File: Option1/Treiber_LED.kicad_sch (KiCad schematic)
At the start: 2 parts, among them Q601 AON6284

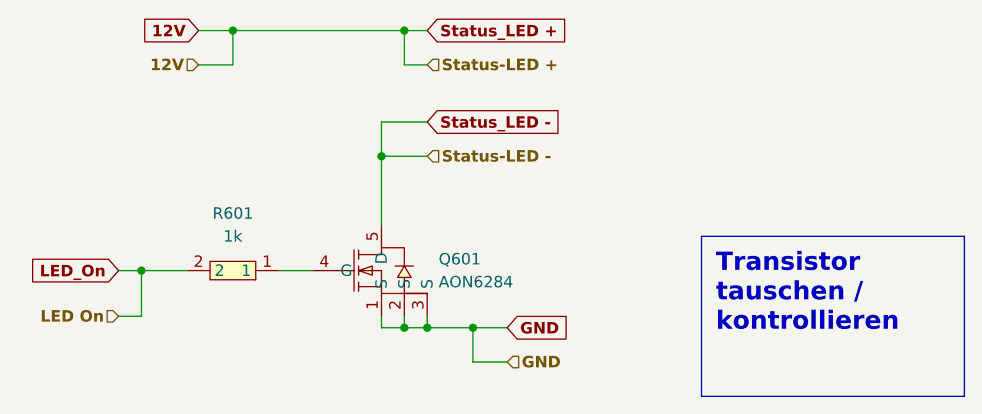
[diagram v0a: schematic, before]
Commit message: SPI Flash hinzugefügt, IN/Outputs vereinheitlicht, USB Flash Möglichkeit hinzugefügt, Display fehtl noch
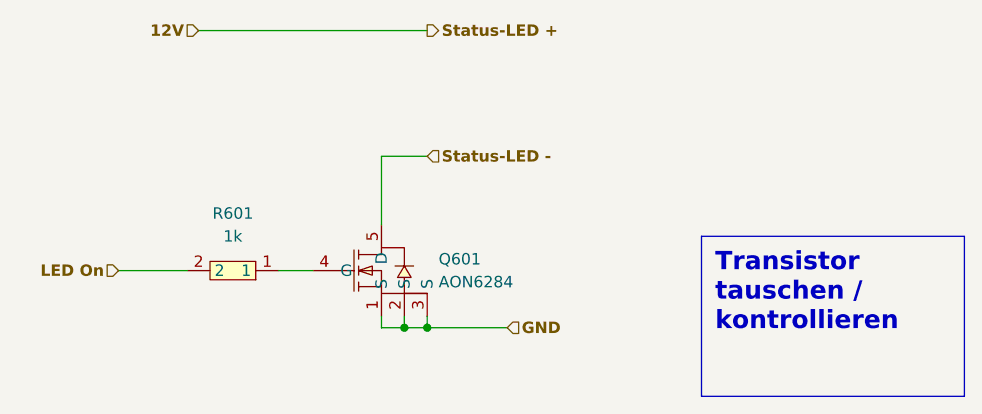
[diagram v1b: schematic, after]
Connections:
- net LED_On renamed LED On
- net Status_LED - renamed Status-LED -

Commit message: USB auf 3V3 umgebaut
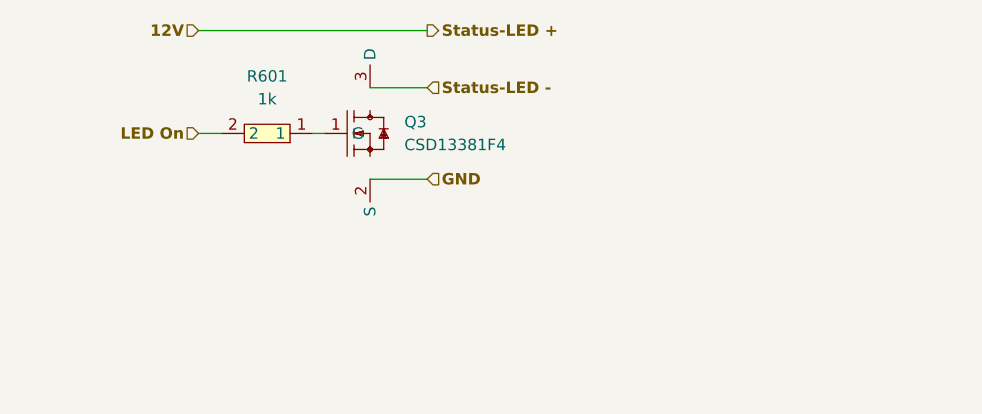
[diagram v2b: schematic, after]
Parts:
- removed Q601: AON6284, easyeda2kicad:POWERVDFN-8_L6.2-W5.2-P1.27-LS6.0-BL, symbol easyeda2kicad:AON6284
- added Q3: CSD13381F4, easyeda2kicad:PICOSTAR-3_L1.0-W0.6-P0.40-S0.65-BL-1, symbol EasyEda2KiCad:CSD13381F4
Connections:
- net GND: now also Q3.2 (S)
- net Status-LED -: now also Q3.3 (D)
- net at R601.1: now also Q3.1 (G)
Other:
- moved on the sheet: R601
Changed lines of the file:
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@@
 		)
 	)
-	(text_box "Transistor tauschen / kontrollieren"
-		(exclude_from_sim no)
-		(at 185.42 96.52 0)
-		(size 29.21 17.78)
-		(margins 1.524 1.524 1.524 1.524)
-		(stroke
-			(width 0)
-			(type default)
-			(color 247 0 0 1)
-		)
-		(fill
-			(type none)
-		)
-		(effects
-			(font
-				(size 2.032 2.032)
-				(thickness 0.4064)
-				(bold yes)
-				(color 247 0 0 1)
-			)
-			(justify left top)
-		)
-	)
-	(junction
-		(at 154.94 106.68)
-		(diameter 0)
-		(color 0 0 0 0)
-	)
-	(junction
-		(at 152.4 106.68)
-		(diameter 0)
-		(color 0 0 0 0)
-	)
-	(wire
-		(pts
-			(xy 154.94 106.68) (xy 152.4 106.68)
-		)
-		(stroke
-			(width 0)
-			(type default)
-		)
-	)
-	(wire
-		(pts
-			(xy 138.43 100.33) (xy 142.24 100.33)
+	(wire
+		(pts
+			(xy 143.51 85.09) (xy 142.24 85.09)
 		)
 		(stroke
@@
 	(wire
 		(pts
-			(xy 152.4 105.41) (xy 152.4 106.68)
-		)
-		(stroke
-			(width 0)
-			(type default)
-		)
-	)
-	(wire
-		(pts
-			(xy 149.86 106.68) (xy 149.86 105.41)
-		)
-		(stroke
-			(width 0)
-			(type default)
-		)
-	)
-	(wire
-		(pts
-			(xy 154.94 105.41) (xy 154.94 106.68)
-		)
-		(stroke
-			(width 0)
-			(type default)
-		)
-	)
-	(wire
-		(pts
-			(xy 152.4 106.68) (xy 149.86 106.68)
-		)
-		(stroke
-			(width 0)
-			(type default)
-		)
-	)
-	(wire
-		(pts
-			(xy 149.86 87.63) (xy 154.94 87.63)
-		)
-		(stroke
-			(width 0)
-			(type default)
-		)
-	)
-	(wire
-		(pts
-			(xy 120.65 100.33) (xy 128.27 100.33)
-		)
-		(stroke
-			(width 0)
-			(type default)
-		)
-	)
-	(wire
-		(pts
-			(xy 154.94 106.68) (xy 163.83 106.68)
-		)
-		(stroke
-			(width 0)
-			(type default)
-		)
-	)
-	(wire
-		(pts
-			(xy 149.86 87.63) (xy 149.86 95.25)
+			(xy 148.59 90.17) (xy 154.94 90.17)
+		)
+		(stroke
+			(width 0)
+			(type default)
+		)
+	)
+	(wire
+		(pts
+			(xy 148.59 80.01) (xy 154.94 80.01)
+		)
+		(stroke
+			(width 0)
+			(type default)
+		)
+	)
+	(wire
+		(pts
+			(xy 129.54 85.09) (xy 132.08 85.09)
 		)
 		(stroke
@@
 	(hierarchical_label "LED On"
 		(shape input)
-		(at 120.65 100.33 180)
+		(at 129.54 85.09 180)
 		(effects
 			(font
@@
 	(hierarchical_label "Status-LED -"
 		(shape input)
-		(at 154.94 87.63 0)
+		(at 154.94 80.01 0)
 		(effects
 			(font
@@
 	(hierarchical_label "GND"
 		(shape input)
-		(at 163.83 106.68 0)
+		(at 154.94 90.17 0)
 		(effects
 			(font
@@
 			)
 			(justify left)
-		)
-	)
-	(symbol
-		(lib_id "easyeda2kicad:AON6284")
-		(at 149.86 100.33 0)
-		(unit 1)
-		(exclude_from_sim no)
-		(in_bom yes)
-		(on_board yes)
-		(dnp no)
-		(fields_autoplaced yes)
-		(property "Reference" "Q601"
-			(at 156.21 99.0599 0)
-			(effects
-				(font
-					(size 1.27 1.27)
-				)
-				(justify left)
-			)
-		)
-		(property "Value" "AON6284"
-			(at 156.21 101.5999 0)
-			(effects
-				(font
-					(size 1.27 1.27)
-				)
-				(justify left)
-			)
-		)
-		(property "Footprint" "easyeda2kicad:POWERVDFN-8_L6.2-W5.2-P1.27-LS6.0-BL"
-			(at 149.86 113.03 0)
-			(effects
-				(font
-					(size 1.27 1.27)
-				)
-				(hide yes)
-			)
-		)
-		(property "Datasheet" ""
-			(at 149.86 100.33 0)
-			(effects
-				(font
-					(size 1.27 1.27)
-				)
-				(hide yes)
-			)
-		)
-		(property "Description" ""
-			(at 149.86 100.33 0)
-			(effects
-				(font
-					(size 1.27 1.27)
-				)
-				(hide yes)
-			)
-		)
-		(property "LCSC Part" "C3277770"
-			(at 149.86 115.57 0)
-			(effects
-				(font
-					(size 1.27 1.27)
-				)
-				(hide yes)
-			)
-		)
-		(pin "4"
-		)
-		(pin "2"
-		)
-		(pin "1"
-		)
-		(pin "3"
-		)
-		(pin "5"
-		)
-		(instances
-			(project "Option1"
-				(path "/b9e5f262-9648-4b79-bdd1-af888b822329/a452be95-5969-43b6-804d-0a34f3106ddf"
-					(reference "Q601")
-					(unit 1)
-				)
-			)
 		)
 	)
 	(symbol
 		(lib_id "easyeda2kicad:0603WAF1001T5E")
-		(at 133.35 100.33 180)
+		(at 137.16 85.09 180)
 		(unit 1)
 		(exclude_from_sim no)
@@
 		(fields_autoplaced yes)
 		(property "Reference" "R601"
-			(at 133.35 93.98 0)
+			(at 137.16 78.74 0)
 			(effects
 				(font
@@
 		)
 		(property "Value" "1k"
-			(at 133.35 96.52 0)
+			(at 137.16 81.28 0)
 			(effects
 				(font
@@
 		)
 		(property "Footprint" "easyeda2kicad:R0603"
-			(at 133.35 92.71 0)
+			(at 137.16 77.47 0)
 			(effects
 				(font
@@
 		)
 		(property "Datasheet" "https://lcsc.com/product-detail/Chip-Resistor-Surface-Mount-UniOhm_1KR-1001-1_C21190.html"
-			(at 133.35 90.17 0)
+			(at 137.16 74.93 0)
 			(effects
 				(font
@@
 		)
 		(property "Description" ""
-			(at 133.35 100.33 0)
+			(at 137.16 85.09 0)
 			(effects
 				(font
@@
 		)
 		(property "LCSC Part" "C21190"
-			(at 133.35 87.63 0)
+			(at 137.16 72.39 0)
 			(effects
 				(font
@@
 					(unit 1)
 				)
+			)
+		)
+	)
+	(symbol
+		(lib_id "EasyEda2KiCad:CSD13381F4")
+		(at 146.05 85.09 0)
+		(unit 1)
+		(exclude_from_sim no)
+		(in_bom yes)
+		(on_board yes)
+		(dnp no)
+		(fields_autoplaced yes)
+		(property "Reference" "Q3"
+			(at 152.4 83.8199 0)
+			(effects
+				(font
+					(size 1.27 1.27)
+				)
+				(justify left)
+			)
+		)
+		(property "Value" "CSD13381F4"
+			(at 152.4 86.3599 0)
+			(effects
+				(font
+					(size 1.27 1.27)
+				)
+				(justify left)
+			)
+		)
+		(property "Footprint" "easyeda2kicad:PICOSTAR-3_L1.0-W0.6-P0.40-S0.65-BL-1"
+			(at 146.05 97.79 0)
+			(effects
+				(font
+					(size 1.27 1.27)
+				)
+				(hide yes)
+			)
+		)
+		(property "Datasheet" ""
+			(at 146.05 85.09 0)
+			(effects
+				(font
+					(size 1.27 1.27)
+				)
+				(hide yes)
+			)
+		)
+		(property "Description" ""
+			(at 146.05 85.09 0)
+			(effects
+				(font
+					(size 1.27 1.27)
+				)
+				(hide yes)
+			)
+		)
+		(property "LCSC Part" "C179868"
+			(at 146.05 100.33 0)
+			(effects
+				(font
+					(size 1.27 1.27)
+				)
+				(hide yes)
+			)
+		)
+		(pin "3"
+		)
+		(pin "1"
+		)
+		(pin "2"
+		)
+		(instances
+			(project "Option1"
+				(path "/b9e5f262-9648-4b79-bdd1-af888b822329/a452be95-5969-43b6-804d-0a34f3106ddf"
+					(reference "Q3")
+					(unit 1)
+				)

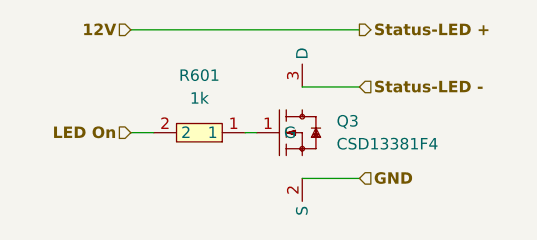
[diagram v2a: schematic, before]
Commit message: Transitor getauscht, Pulldown Widerstände für Definierten LOW Pegel hinzugefügt
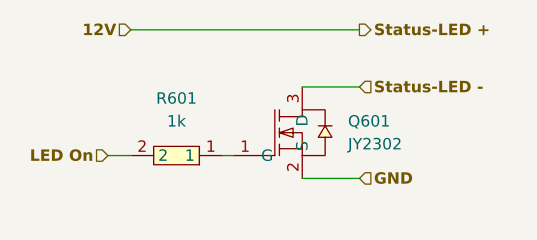
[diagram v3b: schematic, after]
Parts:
- removed Q3: CSD13381F4, easyeda2kicad:PICOSTAR-3_L1.0-W0.6-P0.40-S0.65-BL-1, symbol EasyEda2KiCad:CSD13381F4
- added Q601: JY2302, easyeda2kicad:SOT-23-3_L2.9-W1.3-P0.95-LS2.4-BR, symbol EasyEda2KiCad:JY2302
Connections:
- net GND: now also Q601.2 (S)
- net Status-LED -: now also Q601.3 (D)
- net at R601.1: now also Q601.1 (G)
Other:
- moved on the sheet: R601
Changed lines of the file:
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@@
-	(wire
-		(pts
-			(xy 143.51 85.09) (xy 142.24 85.09)
-		)
-		(stroke
-			(width 0)
-			(type default)
-		)
-	)
 	(wire
 		(pts
@@
 	(wire
 		(pts
-			(xy 129.54 85.09) (xy 132.08 85.09)
+			(xy 127 87.63) (xy 129.54 87.63)
+		)
+		(stroke
+			(width 0)
+			(type default)
+		)
+	)
+	(wire
+		(pts
+			(xy 140.97 87.63) (xy 139.7 87.63)
 		)
 		(stroke
@@
 	(hierarchical_label "LED On"
 		(shape input)
-		(at 129.54 85.09 180)
+		(at 127 87.63 180)
 		(effects
 			(font
@@
 			)
 			(justify left)
+		)
+	)
+	(symbol
+		(lib_id "EasyEda2KiCad:JY2302")
+		(at 146.05 85.09 0)
+		(unit 1)
+		(exclude_from_sim no)
+		(in_bom yes)
+		(on_board yes)
+		(dnp no)
+		(fields_autoplaced yes)
+		(property "Reference" "Q601"
+			(at 153.67 83.8199 0)
+			(effects
+				(font
+					(size 1.27 1.27)
+				)
+				(justify left)
+			)
+		)
+		(property "Value" "JY2302"
+			(at 153.67 86.3599 0)
+			(effects
+				(font
+					(size 1.27 1.27)
+				)
+				(justify left)
+			)
+		)
+		(property "Footprint" "easyeda2kicad:SOT-23-3_L2.9-W1.3-P0.95-LS2.4-BR"
+			(at 146.05 97.79 0)
+			(effects
+				(font
+					(size 1.27 1.27)
+				)
+				(hide yes)
+			)
+		)
+		(property "Datasheet" ""
+			(at 146.05 85.09 0)
+			(effects
+				(font
+					(size 1.27 1.27)
+				)
+				(hide yes)
+			)
+		)
+		(property "Description" ""
+			(at 146.05 85.09 0)
+			(effects
+				(font
+					(size 1.27 1.27)
+				)
+				(hide yes)
+			)
+		)
+		(property "LCSC Part" "C3038095"
+			(at 146.05 100.33 0)
+			(effects
+				(font
+					(size 1.27 1.27)
+				)
+				(hide yes)
+			)
+		)
+		(pin "2"
+		)
+		(pin "1"
+		)
+		(pin "3"
+		)
+		(instances
+			(project ""
+				(path "/b9e5f262-9648-4b79-bdd1-af888b822329/a452be95-5969-43b6-804d-0a34f3106ddf"
+					(reference "Q601")
+					(unit 1)
+				)
+			)
 		)
 	)
 	(symbol
 		(lib_id "easyeda2kicad:0603WAF1001T5E")
-		(at 137.16 85.09 180)
+		(at 134.62 87.63 180)
 		(unit 1)
 		(exclude_from_sim no)
@@
 		(fields_autoplaced yes)
 		(property "Reference" "R601"
-			(at 137.16 78.74 0)
+			(at 134.62 81.28 0)
 			(effects
 				(font
@@
 		)
 		(property "Value" "1k"
-			(at 137.16 81.28 0)
+			(at 134.62 83.82 0)
 			(effects
 				(font
@@
 		)
 		(property "Footprint" "easyeda2kicad:R0603"
-			(at 137.16 77.47 0)
+			(at 134.62 80.01 0)
 			(effects
 				(font
@@
 		)
 		(property "Datasheet" "https://lcsc.com/product-detail/Chip-Resistor-Surface-Mount-UniOhm_1KR-1001-1_C21190.html"
-			(at 137.16 74.93 0)
+			(at 134.62 77.47 0)
 			(effects
 				(font
@@
 		)
 		(property "Description" ""
-			(at 137.16 85.09 0)
+			(at 134.62 87.63 0)
 			(effects
 				(font
@@
 		)
 		(property "LCSC Part" "C21190"
-			(at 137.16 72.39 0)
+			(at 134.62 74.93 0)
 			(effects
 				(font
@@
 					(unit 1)
 				)
-			)
-		)
-	)
-	(symbol
-		(lib_id "EasyEda2KiCad:CSD13381F4")
-		(at 146.05 85.09 0)
-		(unit 1)
-		(exclude_from_sim no)
-		(in_bom yes)
-		(on_board yes)
-		(dnp no)
-		(fields_autoplaced yes)
-		(property "Reference" "Q3"
-			(at 152.4 83.8199 0)
-			(effects
-				(font
-					(size 1.27 1.27)
-				)
-				(justify left)
-			)
-		)
-		(property "Value" "CSD13381F4"
-			(at 152.4 86.3599 0)
-			(effects
-				(font
-					(size 1.27 1.27)
-				)
-				(justify left)
-			)
-		)
-		(property "Footprint" "easyeda2kicad:PICOSTAR-3_L1.0-W0.6-P0.40-S0.65-BL-1"
-			(at 146.05 97.79 0)
-			(effects
-				(font
-					(size 1.27 1.27)
-				)
-				(hide yes)
-			)
-		)
-		(property "Datasheet" ""
-			(at 146.05 85.09 0)
-			(effects
-				(font
-					(size 1.27 1.27)
-				)
-				(hide yes)
-			)
-		)
-		(property "Description" ""
-			(at 146.05 85.09 0)
-			(effects
-				(font
-					(size 1.27 1.27)
-				)
-				(hide yes)
-			)
-		)
-		(property "LCSC Part" "C179868"
-			(at 146.05 100.33 0)
-			(effects
-				(font
-					(size 1.27 1.27)
-				)
-				(hide yes)
-			)
-		)
-		(pin "3"
-		)
-		(pin "1"
-		)
-		(pin "2"
-		)
-		(instances
-			(project "Option1"
-				(path "/b9e5f262-9648-4b79-bdd1-af888b822329/a452be95-5969-43b6-804d-0a34f3106ddf"
-					(reference "Q3")
-					(unit 1)
-				)
